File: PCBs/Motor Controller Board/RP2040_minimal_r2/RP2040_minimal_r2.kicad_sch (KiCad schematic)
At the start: 34 parts, among them J1 USB_B_Micro, J2 Conn_01x02, J3 Conn_02x18_Odd_Even, J4 Conn_02x18_Odd_Even, U1 NCP1117-3.3_SOT223, U2 W25Q128JVS, U3 RP2040, Y1 ABM8-272-T3

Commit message: vault backup: 2025-04-07 20:47:17
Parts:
- added J6: Conn_01x02, symbol Connector_Generic:Conn_01x02
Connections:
- net GND: now also J6.1 (Pin_1)
- new net VM: J6.2 (Pin_2)
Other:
- moved on the sheet: C17, J3, J4

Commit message: vault backup: 2025-04-08 00:30:09
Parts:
- added BTSEL1: SW_Push, Button_Switch_THT:KSA_Tactile_SPST, symbol Switch:SW_Push
- added C18, C20: 0.1u, Capacitor_SMD:C_0603_1608Metric_Pad1.08x0.95mm_HandSolder, symbol Device:C
- added C19, C21: 10u, Capacitor_SMD:CP_Elec_5x5.4, symbol Device:C_Polarized
- added D1, D2: LED, LED_SMD:LED_0603_1608Metric_Pad1.05x0.95mm_HandSolder, symbol Device:LED
- added J5, J7: Conn_01x06_Pin, Connector_PinHeader_2.54mm:PinHeader_1x06_P2.54mm_Vertical, symbol Connector:Conn_01x06_Pin
- added R10, R11: 430, Resistor_SMD:R_0603_1608Metric_Pad0.98x0.95mm_HandSolder, symbol Device:R
- added R6, R9: R, Resistor_SMD:R_0603_1608Metric_Pad0.98x0.95mm_HandSolder, symbol Device:R
- added R7, R8: 2k, Resistor_SMD:R_0603_1608Metric_Pad0.98x0.95mm_HandSolder, symbol Device:R
- added U4, U5: DRV8245HQRXZRQ1, footprints:RXZ0016A-MFG, symbol 2025-04-08_02-58-05:DRV8245HQRXZRQ1
- C1, C17, C4: footprint Capacitor_SMD:C_0805_2012Metric -> Capacitor_SMD:C_0603_1608Metric_Pad1.08x0.95mm_HandSolder
- C10, C11, C12, C13, C14, C15, C16, C2, C3, C5, C6, C7, C8, C9: footprint Capacitor_SMD:C_0402_1005Metric -> Capacitor_SMD:C_0603_1608Metric_Pad1.08x0.95mm_HandSolder
- H1, H2, H3, H4: footprint MountingHole:MountingHole_2.7mm_M2.5 -> MountingHole:MountingHole_3.2mm_M3_DIN965_Pad_TopBottom
- J6: footprint (none) -> Connector_AMASS:AMASS_XT30U-M_1x02_P5.0mm_Vertical
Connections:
- net GPIO12 is gone; now on net +3V3: J3.28 (Pin_28), U3.15 (GPIO12)
- net GPIO17 is gone; now on net +3V3: J4.25 (Pin_25), U3.28 (GPIO17)
- net +3V3: now also J5.4 (Pin_4), J7.4 (Pin_4), R7.1, R7.2, R8.1, R8.2, U4.1 (FAULT_N), U5.1 (FAULT_N)
- net GND: now also BTSEL1.1, C18.1, C19.2, C20.1, C21.2, J5.3 (Pin_3), J7.3 (Pin_3), R10.1, R11.1, R6.1, R9.1, U4.13 (DIAG), U4.15 (ITRIP), U4.16 (MODE), U4.2 (IPROPI), U4.7 (GND), U5.13 (DIAG), U5.15 (ITRIP), U5.16 (MODE), U5.2 (IPROPI), U5.7 (GND)
- net GPIO10: now also U4.3 (SLEEP_N)
- net GPIO11: now also U4.10 (DRVOFF)
- net GPIO13: now also U4.11 (EN_IN1)
- net GPIO14: now also U4.12 (PH_IN2)
- net GPIO15: now also U5.3 (SLEEP_N)
- net GPIO16: now also U5.10 (DRVOFF)
- net GPIO18: now also U5.11 (EN_IN1)
- net GPIO19: now also U5.12 (PH_IN2)
- net GPIO21: now also D1.2 (A)
- net GPIO22: now also D2.2 (A)
- net GPIO6: now also J5.2 (Pin_2)
- net GPIO7: now also J5.1 (Pin_1)
- net GPIO8: now also J7.2 (Pin_2)
- net GPIO9: now also J7.1 (Pin_1)
- net VM: now also C18.2, C19.1, C20.2, C21.1, U4.4 (VM), U5.4 (VM)
- new net: R6.2, U4.14 (SR)
- new net: J5.5 (Pin_5), U4.5 (OUT2), U4.6 (OUT2)
- new net: J5.6 (Pin_6), U4.8 (OUT1), U4.9 (OUT1)
- new net: D1.1 (K), R10.2
- new net: D2.1 (K), R11.2
- new net: R9.2, U5.14 (SR)
- new net: J7.5 (Pin_5), U5.5 (OUT2), U5.6 (OUT2)
- new net: J7.6 (Pin_6), U5.8 (OUT1), U5.9 (OUT1)
- new net USB_BOOT: BTSEL1.2
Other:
- moved on the sheet: C2, C3, J6, R5, Y1

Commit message: PCB Work
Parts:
- removed J3, J4: Conn_02x18_Odd_Even, Connector_PinHeader_2.54mm:PinHeader_2x18_P2.54mm_Vertical, symbol Connector_Generic:Conn_02x18_Odd_Even
- BTSEL1: footprint Button_Switch_THT:KSA_Tactile_SPST -> Button_Switch_THT:SW_PUSH-12mm
- R1, R2, R3, R4, R5: footprint Resistor_SMD:R_0402_1005Metric -> Resistor_SMD:R_0603_1608Metric_Pad0.98x0.95mm_HandSolder
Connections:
- net USB_BOOT is gone; now on net ~{USB_BOOT}: BTSEL1.2
- net +3V3: no longer R7.2, R8.2, U3.15 (GPIO12), U3.28 (GPIO17), U4.1 (FAULT_N), U5.1 (FAULT_N)
- net GPIO11: no longer U4.10 (DRVOFF)
- net GPIO13: now also U4.12 (PH_IN2); no longer U4.11 (EN_IN1)
- net GPIO14: now also U4.11 (EN_IN1); no longer U4.12 (PH_IN2)
- net GPIO15: now also U4.10 (DRVOFF); no longer U5.3 (SLEEP_N)
- net GPIO16: now also U5.3 (SLEEP_N); no longer U5.10 (DRVOFF)
- net GPIO18: now also U5.12 (PH_IN2); no longer U5.11 (EN_IN1)
- net GPIO19: now also U5.11 (EN_IN1); no longer U5.12 (PH_IN2)
- net GPIO20: now also U5.10 (DRVOFF)
- net GPIO6: now also J7.1 (Pin_1); no longer J5.2 (Pin_2)
- net GPIO7: now also J7.2 (Pin_2); no longer J5.1 (Pin_1)
- net GPIO8: now also J5.1 (Pin_1); no longer J7.2 (Pin_2)
- net GPIO9: now also J5.2 (Pin_2); no longer J7.1 (Pin_1)
- net at U5.5 (OUT2), U5.6 (OUT2): now also J7.6 (Pin_6); no longer J7.5 (Pin_5)
- net at U5.8 (OUT1), U5.9 (OUT1): now also J7.5 (Pin_5); no longer J7.6 (Pin_6)
- new net GPIO12: R7.2, U3.15 (GPIO12), U4.1 (FAULT_N)
- new net GPIO17: R8.2, U3.28 (GPIO17), U5.1 (FAULT_N)
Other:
- note removed: "IOs"

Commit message: Oop, I forgor to push
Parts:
- added J4: Conn_01x07, Connector_PinSocket_2.54mm:PinSocket_1x07_P2.54mm_Vertical, symbol Connector_Generic:Conn_01x07
- added J8: Conn_01x06, Connector_PinHeader_2.54mm:PinHeader_1x06_P2.54mm_Vertical, symbol Connector_Generic:Conn_01x06
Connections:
- net GPIO0: now also J8.1 (Pin_1)
- net GPIO1: now also J8.2 (Pin_2)
- net GPIO2: now also J8.3 (Pin_3)
- net GPIO23: now also J4.1 (Pin_1)
- net GPIO24: now also J4.2 (Pin_2)
- net GPIO25: now also J4.3 (Pin_3)
- net GPIO26_ADC0: now also J4.4 (Pin_4)
- net GPIO27_ADC1: now also J4.5 (Pin_5)
- net GPIO28_ADC2: now also J4.6 (Pin_6)
- net GPIO29_ADC3: now also J4.7 (Pin_7)
- net GPIO3: now also J8.4 (Pin_4)
- net GPIO4: now also J8.5 (Pin_5)
- net GPIO5: now also J8.6 (Pin_6)
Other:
- moved on the sheet: D1, D2, R10, R11

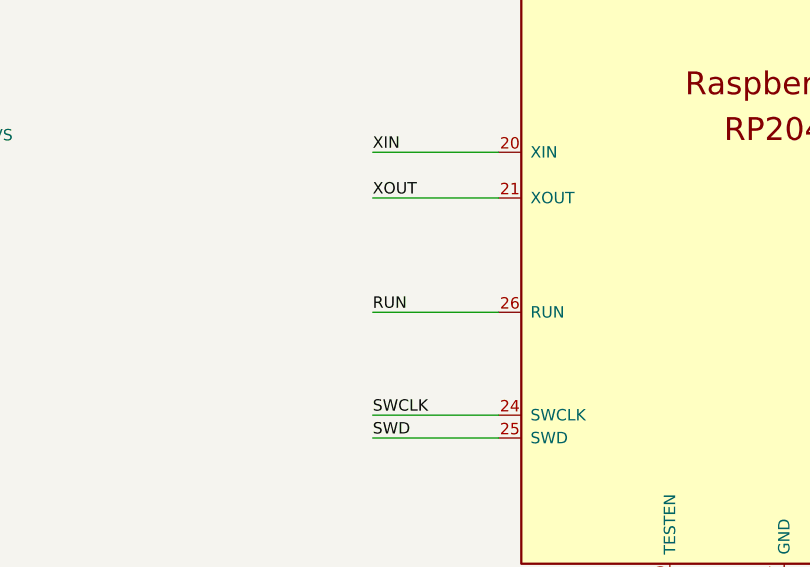
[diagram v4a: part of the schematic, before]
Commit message: RUN tied high
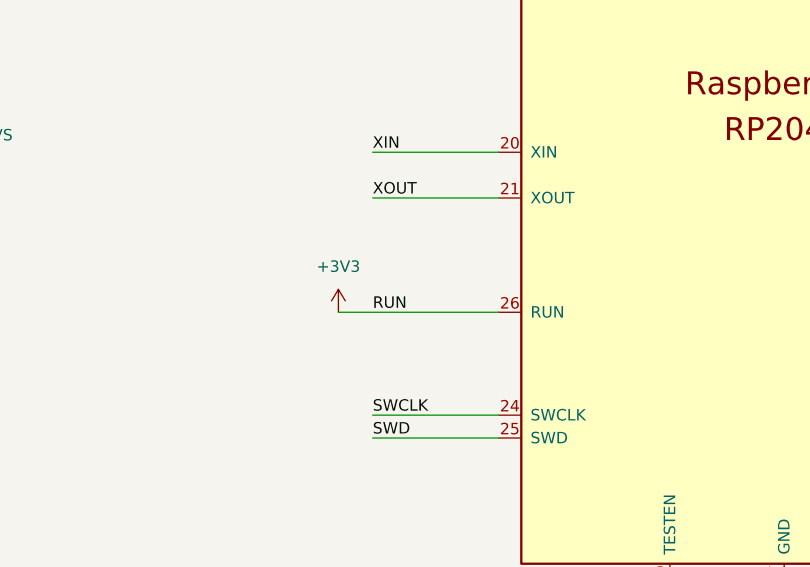
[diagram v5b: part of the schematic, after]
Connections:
- net RUN is gone; now on net +3V3: U3.26 (RUN)
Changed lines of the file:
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@@
 	(wire
 		(pts
-			(xy 166.37 165.1) (xy 152.4 165.1)
-		)
-		(stroke
-			(width 0)
-			(type default)
-		)
-	)
-	(wire
-		(pts
 			(xy 59.69 199.39) (xy 59.69 204.47)
 		)
@@
 	(wire
 		(pts
+			(xy 148.59 165.1) (xy 166.37 165.1)
+		)
+		(stroke
+			(width 0)
+			(type default)
+		)
+	)
+	(wire
+		(pts
 			(xy 234.95 69.85) (xy 234.95 72.39)
 		)
@@
 					(unit 1)
 				)
+			)
+		)
+	)
+	(symbol
+		(lib_name "+3V3_3")
+		(lib_id "power:+3V3")
+		(at 148.59 165.1 0)
+		(unit 1)
+		(exclude_from_sim no)
+		(in_bom yes)
+		(on_board yes)
+		(dnp no)
+		(fields_autoplaced yes)
+		(property "Reference" "#PWR019"
+			(at 148.59 168.91 0)
+			(effects
+				(font
+					(size 1.27 1.27)
+				)
+				(hide yes)
+			)
+		)
+		(property "Value" "+3V3"
+			(at 148.59 160.02 0)
+			(effects
+				(font
+					(size 1.27 1.27)
+				)
+			)
+		)
+		(property "Footprint" ""
+			(at 148.59 165.1 0)
+			(effects
+				(font
+					(size 1.27 1.27)
+				)
+				(hide yes)
+			)
+		)
+		(property "Datasheet" ""
+			(at 148.59 165.1 0)
+			(effects
+				(font
+					(size 1.27 1.27)
+				)
+				(hide yes)
+			)
+		)
+		(property "Description" "Power symbol creates a global label with name \"+3V3\""
+			(at 148.59 165.1 0)
+			(effects
+				(font
+					(size 1.27 1.27)
+				)
+				(hide yes)
+			)
+		)
+		(pin "1"
+		)
+		(instances
+			(project ""
+				(path "/8c0b3d8b-46d3-4173-ab1e-a61765f77d61"
+					(reference "#PWR019")
+					(unit 1)
+				)
